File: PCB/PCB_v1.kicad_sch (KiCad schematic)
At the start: 9 parts, among them J1 Accelerometer, J2 Flysky FS2A Receiver, J3 DC-DC, J4 Battery Left, J5 Battery Right, J6 ESC_Left, J7 ESC_Right, J8 LED, U1 Teensy4.0

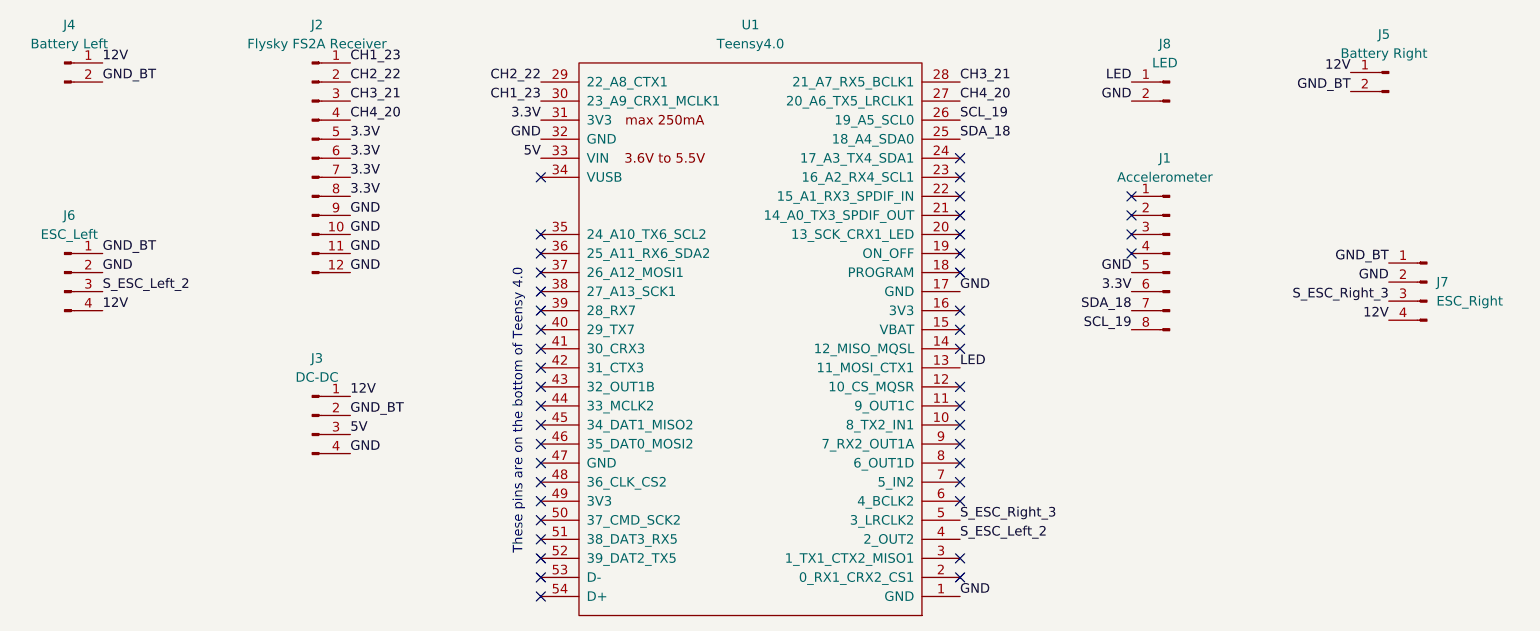
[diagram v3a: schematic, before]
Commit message: Remove the small "GND" from ESC
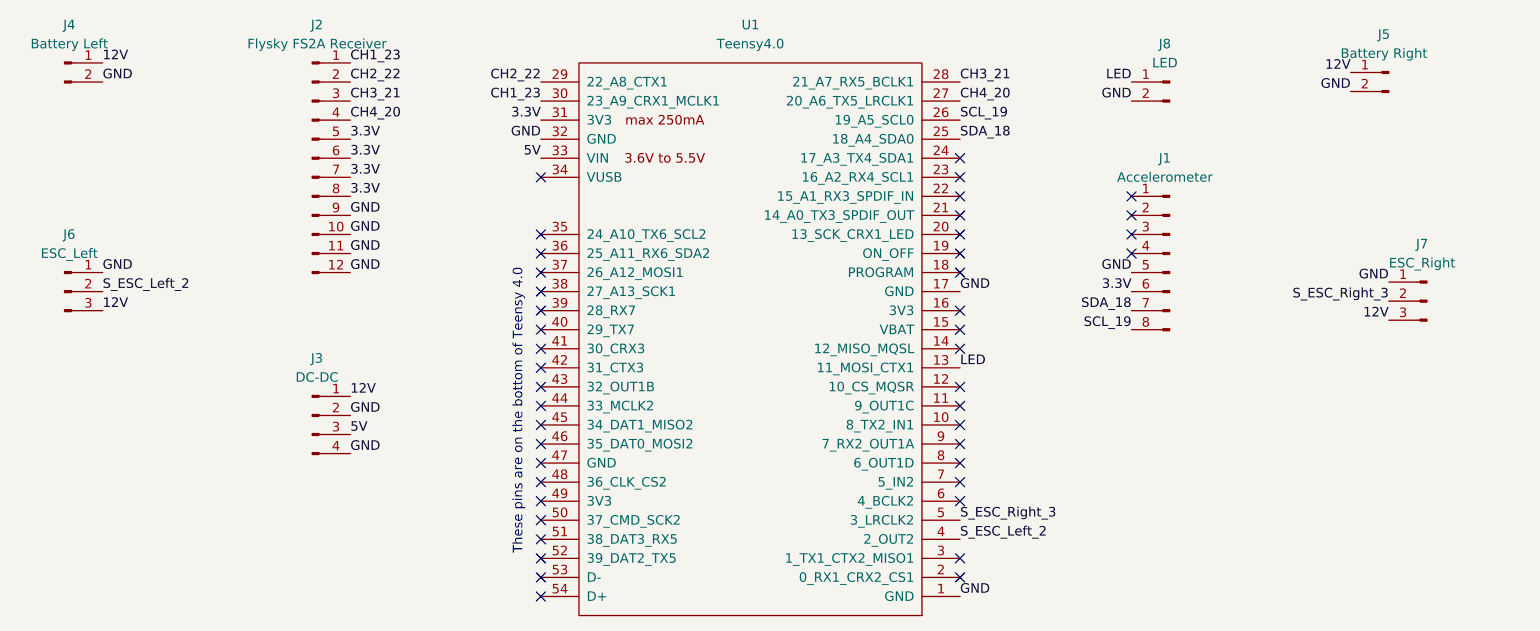
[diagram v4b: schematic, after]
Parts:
- removed J6: ESC_Left, Stuffed Crust:ESC, symbol Connector:Conn_01x04_Pin
- removed J7: ESC_Right, Stuffed Crust:ESC, symbol Connector:Conn_01x04_Pin
- added J6: ESC_Left, Stuffed Crust:ESC, symbol Connector:Conn_01x03_Pin
- added J7: ESC_Right, Stuffed Crust:ESC, symbol Connector:Conn_01x03_Pin
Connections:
- net GND_BT is gone; now on net GND: J3.2 (Pin_2), J4.2 (Pin_2), J5.2 (Pin_2)
- net 12V: now also J6.3 (Pin_3), J7.3 (Pin_3)
- net GND: now also J6.1 (Pin_1), J7.1 (Pin_1)
- net S_ESC_Left_2: now also J6.2 (Pin_2)
- net S_ESC_Right_3: now also J7.2 (Pin_2)
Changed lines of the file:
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@@
-		)
-	)
-	(label "GND_BT"
-		(at 96.52 110.49 0)
-		(effects
-			(font
-				(size 1.27 1.27)
-			)
-			(justify left bottom)
 		)
 	)
@@
 		)
 	)
-	(label "GND_BT"
-		(at 229.87 67.31 180)
-		(effects
-			(font
-				(size 1.27 1.27)
-			)
-			(justify right bottom)
-		)
-	)
 	(label "GND"
 		(at 96.52 91.44 0)
@@
 			)
 			(justify left bottom)
+		)
+	)
+	(label "GND"
+		(at 63.5 91.44 0)
+		(effects
+			(font
+				(size 1.27 1.27)
+			)
+			(justify left bottom)
+		)
+	)
+	(label "GND"
+		(at 234.95 92.71 180)
+		(effects
+			(font
+				(size 1.27 1.27)
+			)
+			(justify right bottom)
 		)
 	)
@@
 		)
 	)
+	(label "GND"
+		(at 96.52 110.49 0)
+		(effects
+			(font
+				(size 1.27 1.27)
+			)
+			(justify left bottom)
+		)
+	)
+	(label "GND"
+		(at 229.87 67.31 180)
+		(effects
+			(font
+				(size 1.27 1.27)
+			)
+			(justify right bottom)
+		)
+	)
 	(label "SCL_19"
 		(at 177.8 71.12 0)
@@
 		)
 	)
-	(label "GND_BT"
-		(at 63.5 88.9 0)
-		(effects
-			(font
-				(size 1.27 1.27)
-			)
-			(justify left bottom)
-		)
-	)
 	(label "12V"
 		(at 234.95 97.79 180)
@@
 		)
 	)
-	(label "GND_BT"
-		(at 234.95 90.17 180)
-		(effects
-			(font
-				(size 1.27 1.27)
-			)
-			(justify right bottom)
-		)
-	)
-	(label "GND"
-		(at 63.5 91.44 0)
-		(effects
-			(font
-				(size 1.27 1.27)
-			)
-			(justify left bottom)
-		)
-	)
 	(label "3.3V"
 		(at 96.52 78.74 0)
@@
 	)
 	(label "GND"
-		(at 234.95 92.71 180)
-		(effects
-			(font
-				(size 1.27 1.27)
-			)
-			(justify right bottom)
+		(at 63.5 66.04 0)
+		(effects
+			(font
+				(size 1.27 1.27)
+			)
+			(justify left bottom)
 		)
 	)
@@
 	(label "S_ESC_Right_3"
 		(at 177.8 124.46 0)
-		(effects
-			(font
-				(size 1.27 1.27)
-			)
-			(justify left bottom)
-		)
-	)
-	(label "GND_BT"
-		(at 63.5 66.04 0)
 		(effects
 			(font
@@
 	)
 	(symbol
+		(lib_id "Connector:Conn_01x03_Pin")
+		(at 58.42 93.98 0)
+		(unit 1)
+		(exclude_from_sim no)
+		(in_bom yes)
+		(on_board yes)
+		(dnp no)
+		(fields_autoplaced yes)
+		(property "Reference" "J6"
+			(at 59.055 86.36 0)
+			(effects
+				(font
+					(size 1.27 1.27)
+				)
+			)
+		)
+		(property "Value" "ESC_Left"
+			(at 59.055 88.9 0)
+			(effects
+				(font
+					(size 1.27 1.27)
+				)
+			)
+		)
+		(property "Footprint" "Stuffed Crust:ESC"
+			(at 58.42 93.98 0)
+			(effects
+				(font
+					(size 1.27 1.27)
+				)
+				(hide yes)
+			)
+		)
+		(property "Datasheet" "~"
+			(at 58.42 93.98 0)
+			(effects
+				(font
+					(size 1.27 1.27)
+				)
+				(hide yes)
+			)
+		)
+		(property "Description" "Generic connector, single row, 01x03, script generated"
+			(at 58.42 93.98 0)
+			(effects
+				(font
+					(size 1.27 1.27)
+				)
+				(hide yes)
+			)
+		)
+		(pin "1"
+		)
+		(pin "2"
+		)
+		(pin "3"
+		)
+		(instances
+			(project ""
+				(path "/be294340-84e5-4c43-afbb-c0b6a21202d8"
+					(reference "J6")
+					(unit 1)
+				)
+			)
+		)
+	)
+	(symbol
 		(lib_id "Connector:Conn_01x02_Pin")
 		(at 58.42 63.5 0)
@@
 	)
 	(symbol
-		(lib_id "Connector:Conn_01x04_Pin")
-		(at 240.03 92.71 0)
+		(lib_id "Connector:Conn_01x03_Pin")
+		(at 240.03 95.25 0)
 		(mirror y)
 		(unit 1)
@@
 		(on_board yes)
 		(dnp no)
-		(fields_autoplaced yes)
 		(property "Reference" "J7"
-			(at 241.3 92.7099 0)
-			(effects
-				(font
-					(size 1.27 1.27)
-				)
-				(justify right)
+			(at 239.395 87.63 0)
+			(effects
+				(font
+					(size 1.27 1.27)
+				)
 			)
 		)
 		(property "Value" "ESC_Right"
-			(at 241.3 95.2499 0)
-			(effects
-				(font
-					(size 1.27 1.27)
-				)
-				(justify right)
+			(at 239.395 90.17 0)
+			(effects
+				(font
+					(size 1.27 1.27)
+				)
 			)
 		)
 		(property "Footprint" "Stuffed Crust:ESC"
-			(at 240.03 92.71 0)
+			(at 240.03 95.25 0)
 			(effects
 				(font
@@
 		)
 		(property "Datasheet" "~"
-			(at 240.03 92.71 0)
-			(effects
-				(font
-					(size 1.27 1.27)
-				)
-				(hide yes)
-			)
-		)
-		(property "Description" "Generic connector, single row, 01x04, script generated"
-			(at 240.03 92.71 0)
-			(effects
-				(font
-					(size 1.27 1.27)
-				)
-				(hide yes)
-			)
+			(at 240.03 95.25 0)
+			(effects
+				(font
+					(size 1.27 1.27)
+				)
+				(hide yes)
+			)
+		)
+		(property "Description" "Generic connector, single row, 01x03, script generated"
+			(at 240.03 95.25 0)
+			(effects
+				(font
+					(size 1.27 1.27)
+				)
+				(hide yes)
+			)
+		)
+		(pin "2"
+		)
+		(pin "1"
 		)
 		(pin "3"
-		)
-		(pin "4"
-		)
-		(pin "1"
-		)
-		(pin "2"
 		)
 		(instances
@@
 					(unit 1)
 				)
-			)
-		)
-	)
-	(symbol
-		(lib_id "Connector:Conn_01x04_Pin")
-		(at 58.42 91.44 0)
-		(unit 1)
-		(exclude_from_sim no)
-		(in_bom yes)
-		(on_board yes)
-		(dnp no)
-		(fields_autoplaced yes)
-		(property "Reference" "J6"
-			(at 59.055 83.82 0)
-			(effects
-				(font
-					(size 1.27 1.27)
-				)
-			)
-		)
-		(property "Value" "ESC_Left"
-			(at 59.055 86.36 0)
-			(effects
-				(font
-					(size 1.27 1.27)
-				)
-			)
-		)
-		(property "Footprint" "Stuffed Crust:ESC"
-			(at 58.42 91.44 0)
-			(effects
-				(font
-					(size 1.27 1.27)
-				)
-				(hide yes)
-			)
-		)
-		(property "Datasheet" "~"
-			(at 58.42 91.44 0)
-			(effects
-				(font
-					(size 1.27 1.27)
-				)
-				(hide yes)
-			)
-		)
-		(property "Description" "Generic connector, single row, 01x04, script generated"
-			(at 58.42 91.44 0)
-			(effects
-				(font
-					(size 1.27 1.27)
-				)
-				(hide yes)
-			)
-		)
-		(pin "4"
-		)
-		(pin "3"
-		)
-		(pin "2"
-		)
-		(pin "1"
-		)
-		(instances
-			(project ""
-				(path "/be294340-84e5-4c43-afbb-c0b6a21202d8"
-					(reference "J6")
-					(unit 1)
-				)

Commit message: Only Keep S Pins for ESCs
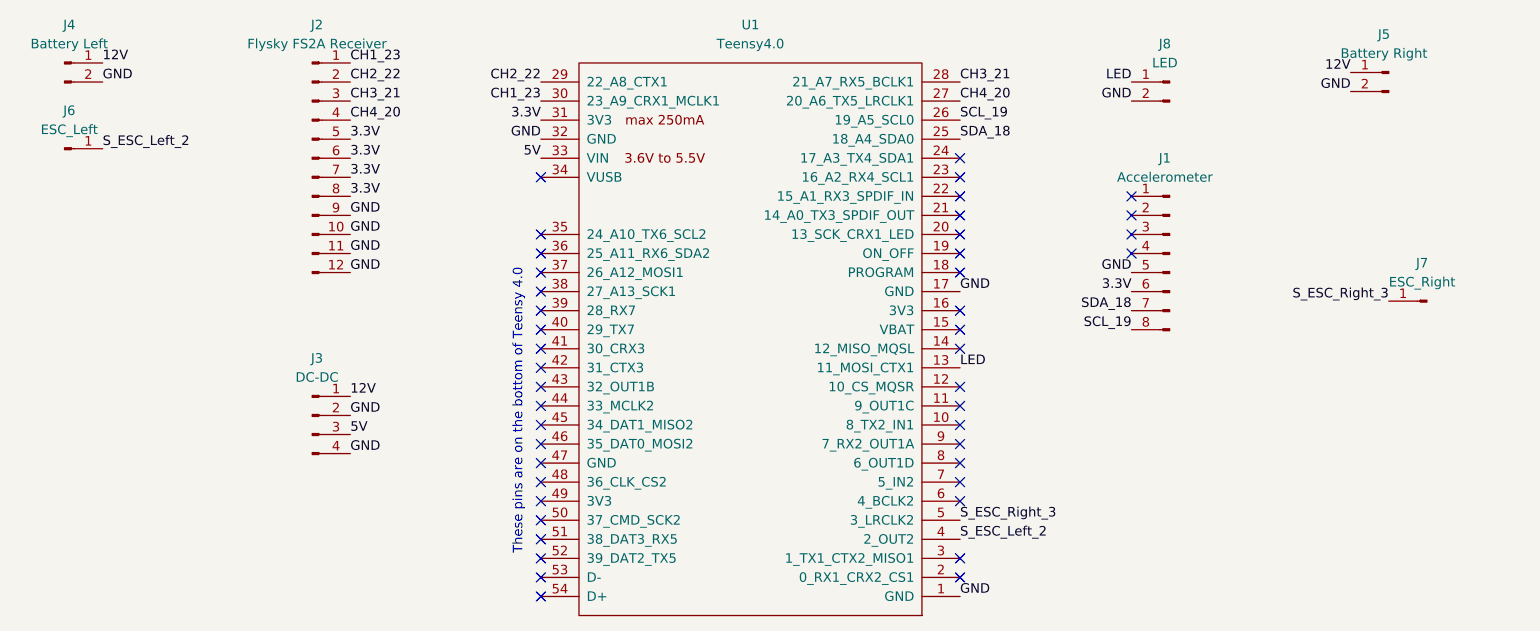
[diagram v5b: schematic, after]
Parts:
- removed J6: ESC_Left, Stuffed Crust:ESC, symbol Connector:Conn_01x03_Pin
- removed J7: ESC_Right, Stuffed Crust:ESC, symbol Connector:Conn_01x03_Pin
- added J6: ESC_Left, Stuffed Crust:ESC, symbol Connector:Conn_01x01_Pin
- added J7: ESC_Right, Stuffed Crust:ESC, symbol Connector:Conn_01x01_Pin
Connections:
- net S_ESC_Left_2: now also J6.1 (Pin_1)
- net S_ESC_Right_3: now also J7.1 (Pin_1)
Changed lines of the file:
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@@
-		)
-	)
-	(label "GND"
-		(at 63.5 91.44 0)
-		(effects
-			(font
-				(size 1.27 1.27)
-			)
-			(justify left bottom)
-		)
-	)
-	(label "GND"
-		(at 234.95 92.71 180)
-		(effects
-			(font
-				(size 1.27 1.27)
-			)
-			(justify right bottom)
 		)
 	)
@@
 		)
 	)
-	(label "12V"
-		(at 234.95 97.79 180)
-		(effects
-			(font
-				(size 1.27 1.27)
-			)
-			(justify right bottom)
-		)
-	)
 	(label "GND"
 		(at 96.52 83.82 0)
@@
 		)
 	)
-	(label "12V"
-		(at 63.5 96.52 0)
-		(effects
-			(font
-				(size 1.27 1.27)
-			)
-			(justify left bottom)
-		)
-	)
 	(label "3.3V"
 		(at 121.92 71.12 180)
@@
 	)
 	(label "S_ESC_Left_2"
-		(at 63.5 93.98 0)
+		(at 63.5 74.93 0)
 		(effects
 			(font
@@
 			)
 			(justify left bottom)
+		)
+	)
+	(symbol
+		(lib_id "Connector:Conn_01x01_Pin")
+		(at 240.03 95.25 0)
+		(mirror y)
+		(unit 1)
+		(exclude_from_sim no)
+		(in_bom yes)
+		(on_board yes)
+		(dnp no)
+		(fields_autoplaced yes)
+		(property "Reference" "J7"
+			(at 239.395 90.17 0)
+			(effects
+				(font
+					(size 1.27 1.27)
+				)
+			)
+		)
+		(property "Value" "ESC_Right"
+			(at 239.395 92.71 0)
+			(effects
+				(font
+					(size 1.27 1.27)
+				)
+			)
+		)
+		(property "Footprint" "Stuffed Crust:ESC"
+			(at 240.03 95.25 0)
+			(effects
+				(font
+					(size 1.27 1.27)
+				)
+				(hide yes)
+			)
+		)
+		(property "Datasheet" "~"
+			(at 240.03 95.25 0)
+			(effects
+				(font
+					(size 1.27 1.27)
+				)
+				(hide yes)
+			)
+		)
+		(property "Description" "Generic connector, single row, 01x01, script generated"
+			(at 240.03 95.25 0)
+			(effects
+				(font
+					(size 1.27 1.27)
+				)
+				(hide yes)
+			)
+		)
+		(pin "1"
+		)
+		(instances
+			(project ""
+				(path "/be294340-84e5-4c43-afbb-c0b6a21202d8"
+					(reference "J7")
+					(unit 1)
+				)
+			)
+		)
+	)
+	(symbol
+		(lib_id "Connector:Conn_01x01_Pin")
+		(at 58.42 74.93 0)
+		(unit 1)
+		(exclude_from_sim no)
+		(in_bom yes)
+		(on_board yes)
+		(dnp no)
+		(fields_autoplaced yes)
+		(property "Reference" "J6"
+			(at 59.055 69.85 0)
+			(effects
+				(font
+					(size 1.27 1.27)
+				)
+			)
+		)
+		(property "Value" "ESC_Left"
+			(at 59.055 72.39 0)
+			(effects
+				(font
+					(size 1.27 1.27)
+				)
+			)
+		)
+		(property "Footprint" "Stuffed Crust:ESC"
+			(at 58.42 74.93 0)
+			(effects
+				(font
+					(size 1.27 1.27)
+				)
+				(hide yes)
+			)
+		)
+		(property "Datasheet" "~"
+			(at 58.42 74.93 0)
+			(effects
+				(font
+					(size 1.27 1.27)
+				)
+				(hide yes)
+			)
+		)
+		(property "Description" "Generic connector, single row, 01x01, script generated"
+			(at 58.42 74.93 0)
+			(effects
+				(font
+					(size 1.27 1.27)
+				)
+				(hide yes)
+			)
+		)
+		(pin "1"
+		)
+		(instances
+			(project ""
+				(path "/be294340-84e5-4c43-afbb-c0b6a21202d8"
+					(reference "J6")
+					(unit 1)
+				)
+			)
 		)
 	)
@@
 	)
 	(symbol
-		(lib_id "Connector:Conn_01x03_Pin")
-		(at 58.42 93.98 0)
-		(unit 1)
-		(exclude_from_sim no)
-		(in_bom yes)
-		(on_board yes)
-		(dnp no)
-		(fields_autoplaced yes)
-		(property "Reference" "J6"
-			(at 59.055 86.36 0)
-			(effects
-				(font
-					(size 1.27 1.27)
-				)
-			)
-		)
-		(property "Value" "ESC_Left"
-			(at 59.055 88.9 0)
-			(effects
-				(font
-					(size 1.27 1.27)
-				)
-			)
-		)
-		(property "Footprint" "Stuffed Crust:ESC"
-			(at 58.42 93.98 0)
-			(effects
-				(font
-					(size 1.27 1.27)
-				)
-				(hide yes)
-			)
-		)
-		(property "Datasheet" "~"
-			(at 58.42 93.98 0)
-			(effects
-				(font
-					(size 1.27 1.27)
-				)
-				(hide yes)
-			)
-		)
-		(property "Description" "Generic connector, single row, 01x03, script generated"
-			(at 58.42 93.98 0)
-			(effects
-				(font
-					(size 1.27 1.27)
-				)
-				(hide yes)
-			)
-		)
-		(pin "1"
-		)
-		(pin "2"
-		)
-		(pin "3"
-		)
-		(instances
-			(project ""
-				(path "/be294340-84e5-4c43-afbb-c0b6a21202d8"
-					(reference "J6")
-					(unit 1)
-				)
-			)
-		)
-	)
-	(symbol
 		(lib_id "Connector:Conn_01x02_Pin")
 		(at 58.42 63.5 0)
@@
 					(unit 1)
 				)
-			)
-		)
-	)
-	(symbol
-		(lib_id "Connector:Conn_01x03_Pin")
-		(at 240.03 95.25 0)
-		(mirror y)
-		(unit 1)
-		(exclude_from_sim no)
-		(in_bom yes)
-		(on_board yes)
-		(dnp no)
-		(property "Reference" "J7"
-			(at 239.395 87.63 0)
-			(effects
-				(font
-					(size 1.27 1.27)
-				)
-			)
-		)
-		(property "Value" "ESC_Right"
-			(at 239.395 90.17 0)
-			(effects
-				(font
-					(size 1.27 1.27)
-				)
-			)
-		)
-		(property "Footprint" "Stuffed Crust:ESC"
-			(at 240.03 95.25 0)
-			(effects
-				(font
-					(size 1.27 1.27)
-				)
-				(hide yes)
-			)
-		)
-		(property "Datasheet" "~"
-			(at 240.03 95.25 0)
-			(effects
-				(font
-					(size 1.27 1.27)
-				)
-				(hide yes)
-			)
-		)
-		(property "Description" "Generic connector, single row, 01x03, script generated"
-			(at 240.03 95.25 0)
-			(effects
-				(font
-					(size 1.27 1.27)
-				)
-				(hide yes)
-			)
-		)
-		(pin "2"
-		)
-		(pin "1"
-		)
-		(pin "3"
-		)
-		(instances
-			(project ""
-				(path "/be294340-84e5-4c43-afbb-c0b6a21202d8"
-					(reference "J7")
-					(unit 1)
-				)
